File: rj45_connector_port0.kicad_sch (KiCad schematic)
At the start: 4 parts, among them J1 RJ45_1840888-1

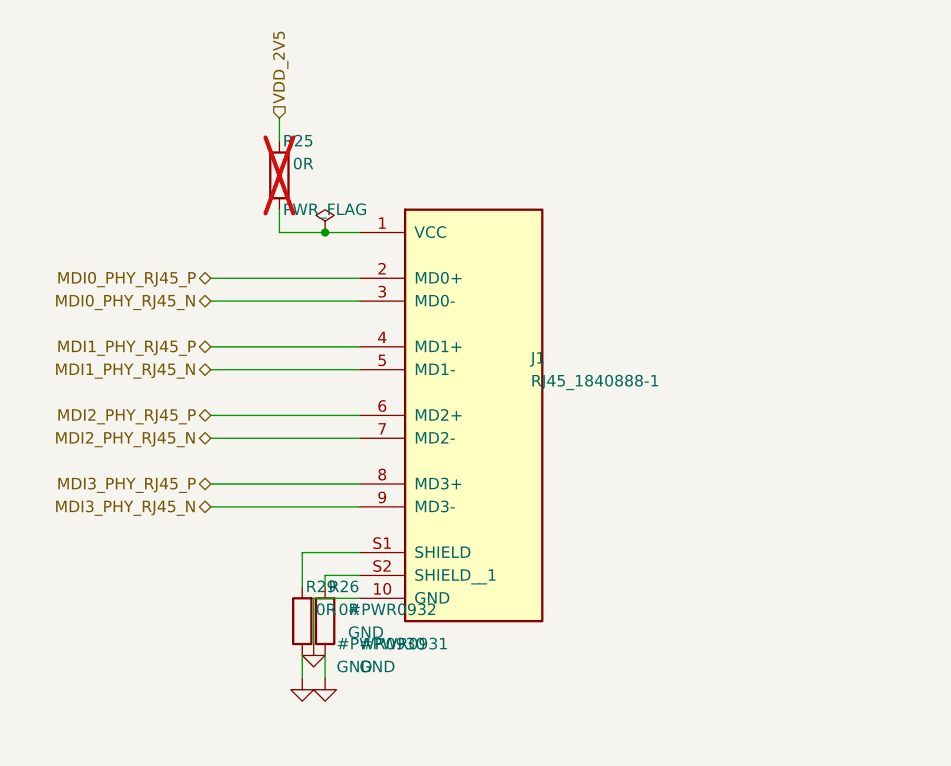
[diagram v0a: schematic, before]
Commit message: Improve schematic readability across all sheets
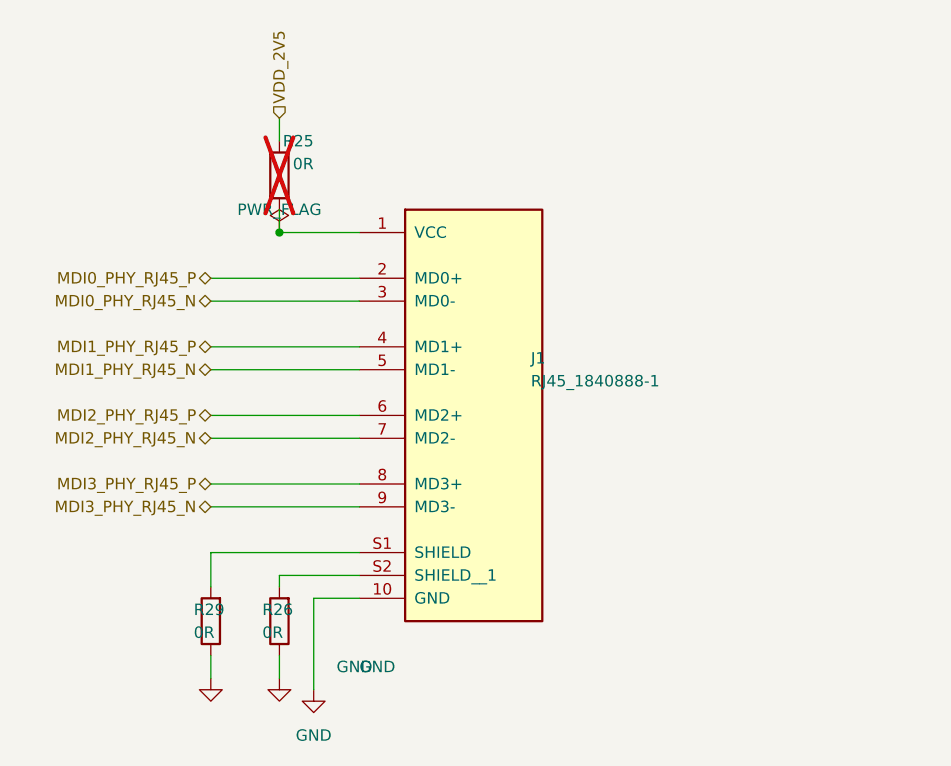
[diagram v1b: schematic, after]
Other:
- moved on the sheet: R26, R29
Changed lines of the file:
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@@
 	(wire
 		(pts
-			(xy 149.86 93.98) (xy 143.51 93.98)
-		)
-		(stroke
-			(width 0)
-			(type default)
-		)
-	)
-	(wire
-		(pts
-			(xy 149.86 96.52) (xy 146.05 96.52)
-		)
-		(stroke
-			(width 0)
-			(type default)
-		)
-	)
-	(wire
-		(pts
-			(xy 143.51 93.98) (xy 143.51 97.79)
+			(xy 149.86 93.98) (xy 133.35 93.98)
+		)
+		(stroke
+			(width 0)
+			(type default)
+		)
+	)
+	(wire
+		(pts
+			(xy 149.86 96.52) (xy 140.97 96.52)
+		)
+		(stroke
+			(width 0)
+			(type default)
+		)
+	)
+	(wire
+		(pts
+			(xy 133.35 93.98) (xy 133.35 97.79)
 		)
 		(stroke
@@
 	(symbol
 		(lib_id "KL_R:R_0R_0.063W_5pct_0402")
-		(at 143.51 101.6 180)
+		(at 133.35 101.6 180)
 		(unit 1)
 		(exclude_from_sim no)
@@
 		(dnp no)
 		(property "Reference" "R29"
-			(at 147.32 97.79 0)
-			(effects
-				(font
-					(size 1.27 1.27)
-				)
-				(justify left)
+			(at 131.45 100.33 0)
+			(effects
+				(font
+					(size 1.27 1.27)
+				)
+				(justify right)
 			)
 		)
 		(property "Value" "0R"
-			(at 147.32 100.33 0)
-			(effects
-				(font
-					(size 1.27 1.27)
-				)
-				(justify left)
+			(at 131.45 102.87 0)
+			(effects
+				(font
+					(size 1.27 1.27)
+				)
+				(justify right)
 			)
 		)
@@
 	(wire
 		(pts
-			(xy 143.51 105.41) (xy 143.51 107.95)
+			(xy 133.35 105.41) (xy 133.35 107.95)
 		)
 		(stroke
@@
 	(symbol
 		(lib_id "power:GND")
-		(at 143.51 107.95 0)
+		(at 133.35 107.95 0)
 		(unit 1)
 		(exclude_from_sim no)
@@
 		(property "Reference" "#PWR0930"
 			(at 147.32 104.14 0)
+			(hide yes)
 			(effects
 				(font
@@
 	(wire
 		(pts
-			(xy 146.05 96.52) (xy 146.05 97.79)
+			(xy 140.97 96.52) (xy 140.97 97.79)
 		)
 		(stroke
@@
 	(symbol
 		(lib_id "KL_R:R_0R_0.063W_5pct_0402")
-		(at 146.05 101.6 180)
+		(at 140.97 101.6 180)
 		(unit 1)
 		(exclude_from_sim no)
@@
 		(dnp no)
 		(property "Reference" "R26"
-			(at 149.86 97.79 0)
-			(effects
-				(font
-					(size 1.27 1.27)
-				)
-				(justify left)
+			(at 139.07 100.33 0)
+			(effects
+				(font
+					(size 1.27 1.27)
+				)
+				(justify right)
 			)
 		)
 		(property "Value" "0R"
-			(at 149.86 100.33 0)
-			(effects
-				(font
-					(size 1.27 1.27)
-				)
-				(justify left)
+			(at 139.07 102.87 0)
+			(effects
+				(font
+					(size 1.27 1.27)
+				)
+				(justify right)
 			)
 		)
@@
 	(wire
 		(pts
-			(xy 146.05 105.41) (xy 146.05 107.95)
+			(xy 140.97 105.41) (xy 140.97 107.95)
 		)
 		(stroke
@@
 	(symbol
 		(lib_id "power:GND")
-		(at 146.05 107.95 0)
+		(at 140.97 107.95 0)
 		(unit 1)
 		(exclude_from_sim no)
@@
 		(property "Reference" "#PWR0931"
 			(at 149.86 104.14 0)
+			(hide yes)
 			(effects
 				(font
@@
 	(wire
 		(pts
-			(xy 144.78 99.06) (xy 144.78 104.14)
+			(xy 144.78 99.06) (xy 144.78 109.22)
 		)
 		(stroke
@@
 	(symbol
 		(lib_id "power:GND")
-		(at 144.78 104.14 0)
+		(at 144.78 109.22 0)
 		(unit 1)
 		(exclude_from_sim no)
@@
 		(property "Reference" "#PWR0932"
 			(at 148.59 100.33 0)
+			(hide yes)
 			(effects
 				(font
@@
 		)
 		(property "Value" "GND"
-			(at 148.59 102.87 0)
-			(effects
-				(font
-					(size 1.27 1.27)
-				)
-				(justify left)
+			(at 144.78 114.3 0)
+			(effects
+				(font
+					(size 1.27 1.27)
+				)
 			)
 		)
@@
 	(symbol
 		(lib_id "KL_Flags:PWR_FLAG")
-		(at 146.05 58.42 0)
+		(at 140.97 58.42 0)
 		(unit 1)
 		(exclude_from_sim no)
@@
 		(dnp no)
 		(property "Reference" "#FLG0901"
-			(at 146.05 54.61 0)
+			(at 140.97 54.61 0)
 			(hide yes)
 			(effects
@@
 		)
 		(property "Value" "PWR_FLAG"
-			(at 146.05 55.88 0)
+			(at 140.97 55.88 0)
 			(effects
 				(font
@@
 	)
 	(junction
-		(at 146.05 58.42)
+		(at 140.97 58.42)
 		(diameter 0)
 		(color 0 0 0 0)

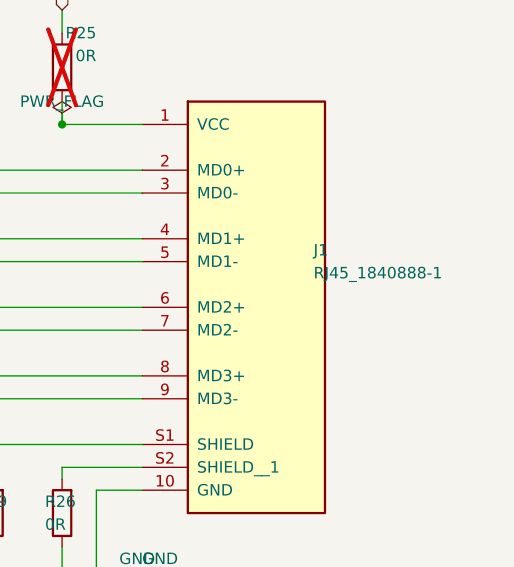
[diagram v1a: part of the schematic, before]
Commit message: Migrate RJ45 port0 sheet to KiCad 10 file format
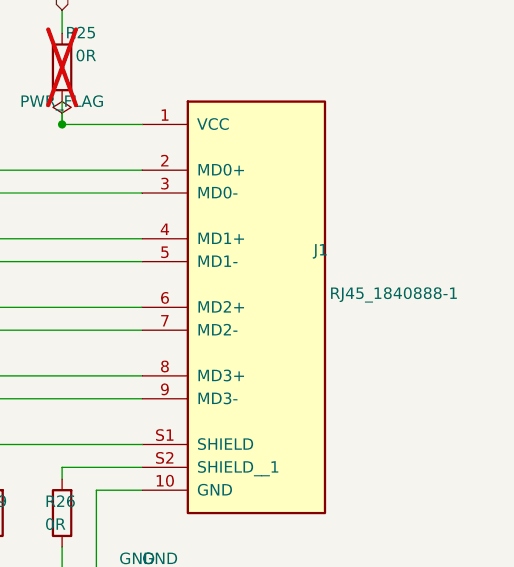
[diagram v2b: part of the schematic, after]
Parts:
- J1: Digikey TBD -> 5923-1840888-1-ND; LCSC TBD -> C5876366
- R25, R26, R29: Digikey TBD -> 541-4062-1-ND; LCSC TBD -> C844710
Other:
- company: (none) -> Kebag Logic: kebag-logic.com
- title: (none) -> RJ45 Connector Port 0

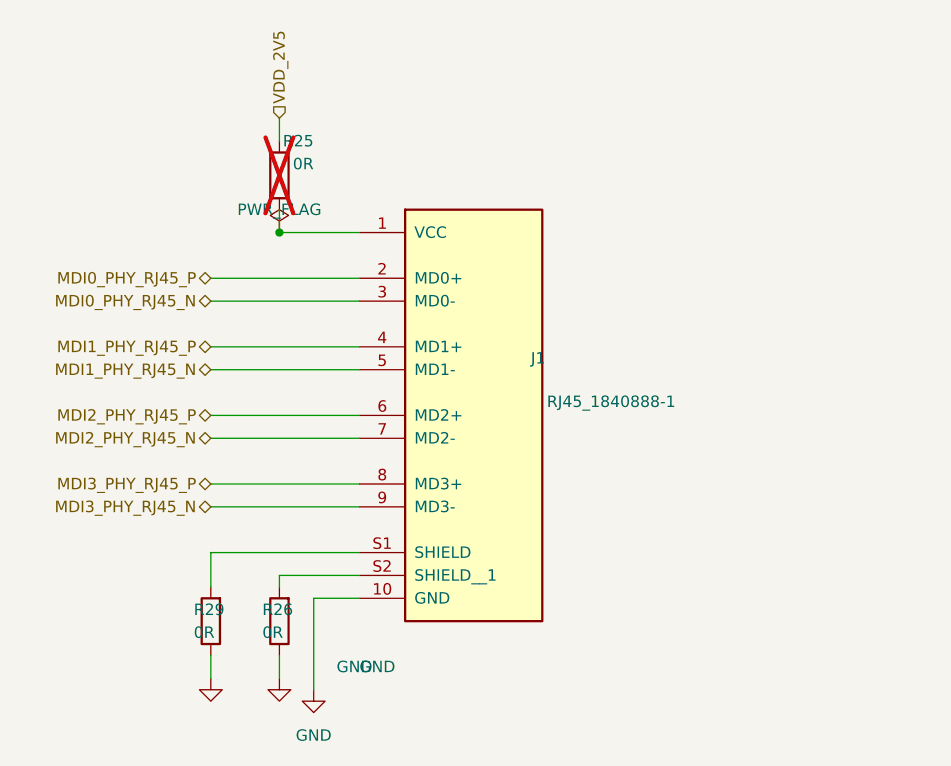
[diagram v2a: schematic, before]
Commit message: Add chassis isolation, remove magjack centre-tap resistor
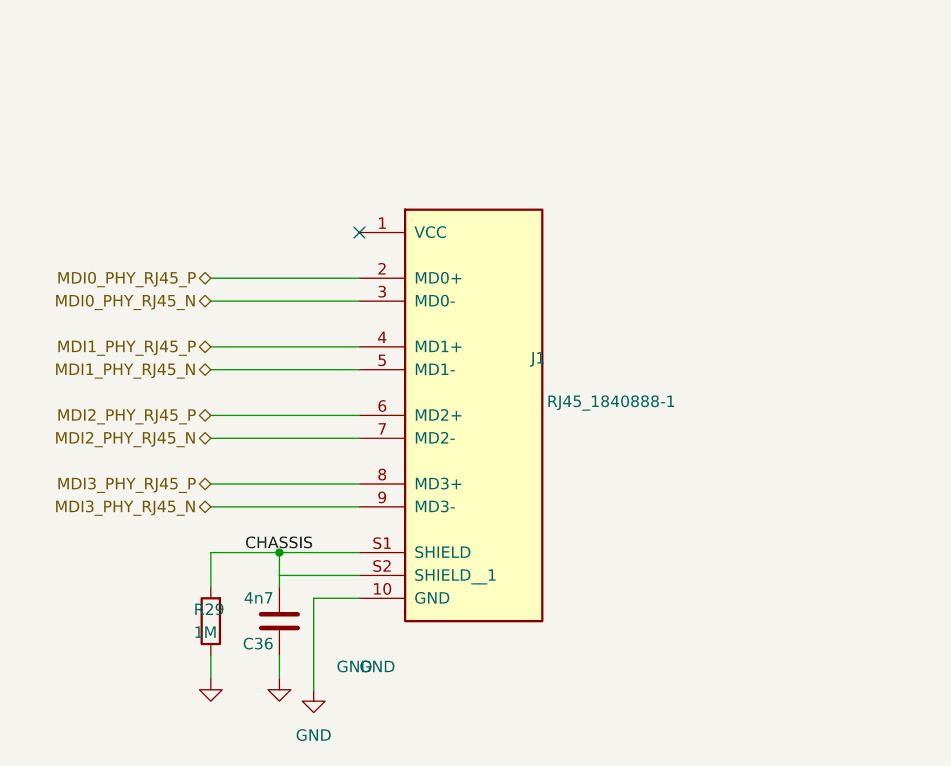
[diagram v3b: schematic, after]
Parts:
- removed R25, R26: 0R, KL_Footprints:R_0402, symbol KL_R:R_0R_0.063W_5pct_0402
- added C36: 4n7, KL_Footprints:C_1210, symbol KL_C:C_4n7_2kV_10pct_X7R_1210
- R29: value 0R -> 1M; footprint KL_Footprints:R_0402 -> KL_Footprints:R_1206; symbol KL_R:R_0R_0.063W_5pct_0402 -> KL_R:R_1M_0.25W_1pct_1206; Digikey 541-4062-1-ND -> (none); LCSC C844710 -> C844869; MPN CRCW04020000Z0EDC -> CRCW12061M00FKEA; Mouser 71-CRCW04020000Z0EDC -> (none); Package_in_inch 0402 -> 1206; Power_in_W 0.063 -> 0.25; Tolerance_in_pct 5 -> 1
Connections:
- net GND: now also C36.1
- net CHASSIS: now reaches J1.S1 (SHIELD), R29.2
- net CHASSIS: now also J1.S2 (SHIELD__1), C36.2
- no-connect marks 0 -> 1

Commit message: Mirror J1 MDI pins, add LED_0 mirror-mode strap
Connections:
- net MDI0_PHY_RJ45_N: now also J1.8 (MD3+); no longer J1.3 (MD0-)
- net MDI0_PHY_RJ45_P: now also J1.9 (MD3-); no longer J1.2 (MD0+)
- net MDI1_PHY_RJ45_N: now also J1.6 (MD2+); no longer J1.5 (MD1-)
- net MDI1_PHY_RJ45_P: now also J1.7 (MD2-); no longer J1.4 (MD1+)
- net MDI2_PHY_RJ45_N: now also J1.4 (MD1+); no longer J1.7 (MD2-)
- net MDI2_PHY_RJ45_P: now also J1.5 (MD1-); no longer J1.6 (MD2+)
- net MDI3_PHY_RJ45_N: now also J1.2 (MD0+); no longer J1.9 (MD3-)
- net MDI3_PHY_RJ45_P: now also J1.3 (MD0-); no longer J1.8 (MD3+)
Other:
- note added: "J1 is mounted on B.Cu (bottom), so its pin row is mirrored. MDI pairs are mapped A<->D, B<->C with P/N swapped ON PURPOSE: the DP83867 RJ45 mirror mode (LED_0 strap mode 3, R31/R32 on the PHY sheet; datasheet 7.4.6.6) undoes it inside the PHY. Do not "fix" this mapping without removing the strap."
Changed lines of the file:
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@@
 		)
 	)
-	(hierarchical_label "MDI2_PHY_RJ45_P"
-		(shape bidirectional)
-		(at 133.35 78.74 180)
-		(effects
-			(font
-				(size 1.27 1.27)
-			)
-			(justify right)
-		)
-	)
-	(hierarchical_label "MDI2_PHY_RJ45_N"
-		(shape bidirectional)
-		(at 133.35 81.28 180)
-		(effects
-			(font
-				(size 1.27 1.27)
-			)
-			(justify right)
-		)
-	)
-	(hierarchical_label "MDI1_PHY_RJ45_N"
-		(shape bidirectional)
-		(at 133.35 73.66 180)
-		(effects
-			(font
-				(size 1.27 1.27)
-			)
-			(justify right)
-		)
-	)
-	(hierarchical_label "MDI0_PHY_RJ45_N"
-		(shape bidirectional)
-		(at 133.35 66.04 180)
-		(effects
-			(font
-				(size 1.27 1.27)
-			)
-			(justify right)
-		)
-	)
-	(hierarchical_label "MDI1_PHY_RJ45_P"
-		(shape bidirectional)
-		(at 133.35 71.12 180)
-		(effects
-			(font
-				(size 1.27 1.27)
-			)
-			(justify right)
-		)
-	)
-	(hierarchical_label "MDI0_PHY_RJ45_P"
+	(hierarchical_label "MDI3_PHY_RJ45_N"
 		(shape bidirectional)
 		(at 133.35 63.5 180)
@@
 	(hierarchical_label "MDI3_PHY_RJ45_P"
 		(shape bidirectional)
+		(at 133.35 66.04 180)
+		(effects
+			(font
+				(size 1.27 1.27)
+			)
+			(justify right)
+		)
+	)
+	(hierarchical_label "MDI2_PHY_RJ45_N"
+		(shape bidirectional)
+		(at 133.35 71.12 180)
+		(effects
+			(font
+				(size 1.27 1.27)
+			)
+			(justify right)
+		)
+	)
+	(hierarchical_label "MDI2_PHY_RJ45_P"
+		(shape bidirectional)
+		(at 133.35 73.66 180)
+		(effects
+			(font
+				(size 1.27 1.27)
+			)
+			(justify right)
+		)
+	)
+	(hierarchical_label "MDI1_PHY_RJ45_N"
+		(shape bidirectional)
+		(at 133.35 78.74 180)
+		(effects
+			(font
+				(size 1.27 1.27)
+			)
+			(justify right)
+		)
+	)
+	(hierarchical_label "MDI1_PHY_RJ45_P"
+		(shape bidirectional)
+		(at 133.35 81.28 180)
+		(effects
+			(font
+				(size 1.27 1.27)
+			)
+			(justify right)
+		)
+	)
+	(hierarchical_label "MDI0_PHY_RJ45_N"
+		(shape bidirectional)
 		(at 133.35 86.36 180)
 		(effects
@@
 		)
 	)
-	(hierarchical_label "MDI3_PHY_RJ45_N"
+	(hierarchical_label "MDI0_PHY_RJ45_P"
 		(shape bidirectional)
 		(at 133.35 88.9 180)
@@
 		)
 	)
+  (text "J1 is mounted on B.Cu (bottom), so its pin row is mirrored.\nMDI pairs are mapped A<->D, B<->C with P/N swapped ON PURPOSE:\nthe DP83867 RJ45 mirror mode (LED_0 strap mode 3, R31/R32 on the\nPHY sheet; datasheet 7.4.6.6) undoes it inside the PHY.\nDo not \"fix\" this mapping without removing the strap."
+    (at 132.08 45.72 0)
+    (effects (font (size 1.27 1.27)) (justify left bottom))
+  )
 	(symbol
 		(lib_id "power:GND")

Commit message: Switch BOM to in-stock LCSC parts, U3 to TLV73311
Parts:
- C36: LCSC (none) -> C2167834
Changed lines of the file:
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@@
 			)
 		)
-		(property "Datasheet" "https://content.kemet.com/datasheets/KEM_C1010_X7R_HV_SMD.pdf"
+		(property "Datasheet" "https://www.lcsc.com/datasheet/lcsc_datasheet_2410121737_KEMET-C1210C472KGRACTU_C2167834.pdf"
 			(at 140.97 101.6 0)
 			(hide yes)
@@
 			)
 		)
-		(property "LCSC" ""
+		(property "LCSC" "C2167834"
 			(at 140.97 101.6 0)
 			(hide yes)
